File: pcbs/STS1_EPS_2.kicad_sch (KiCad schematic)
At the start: 1 part, among them J1 Inter-EPS

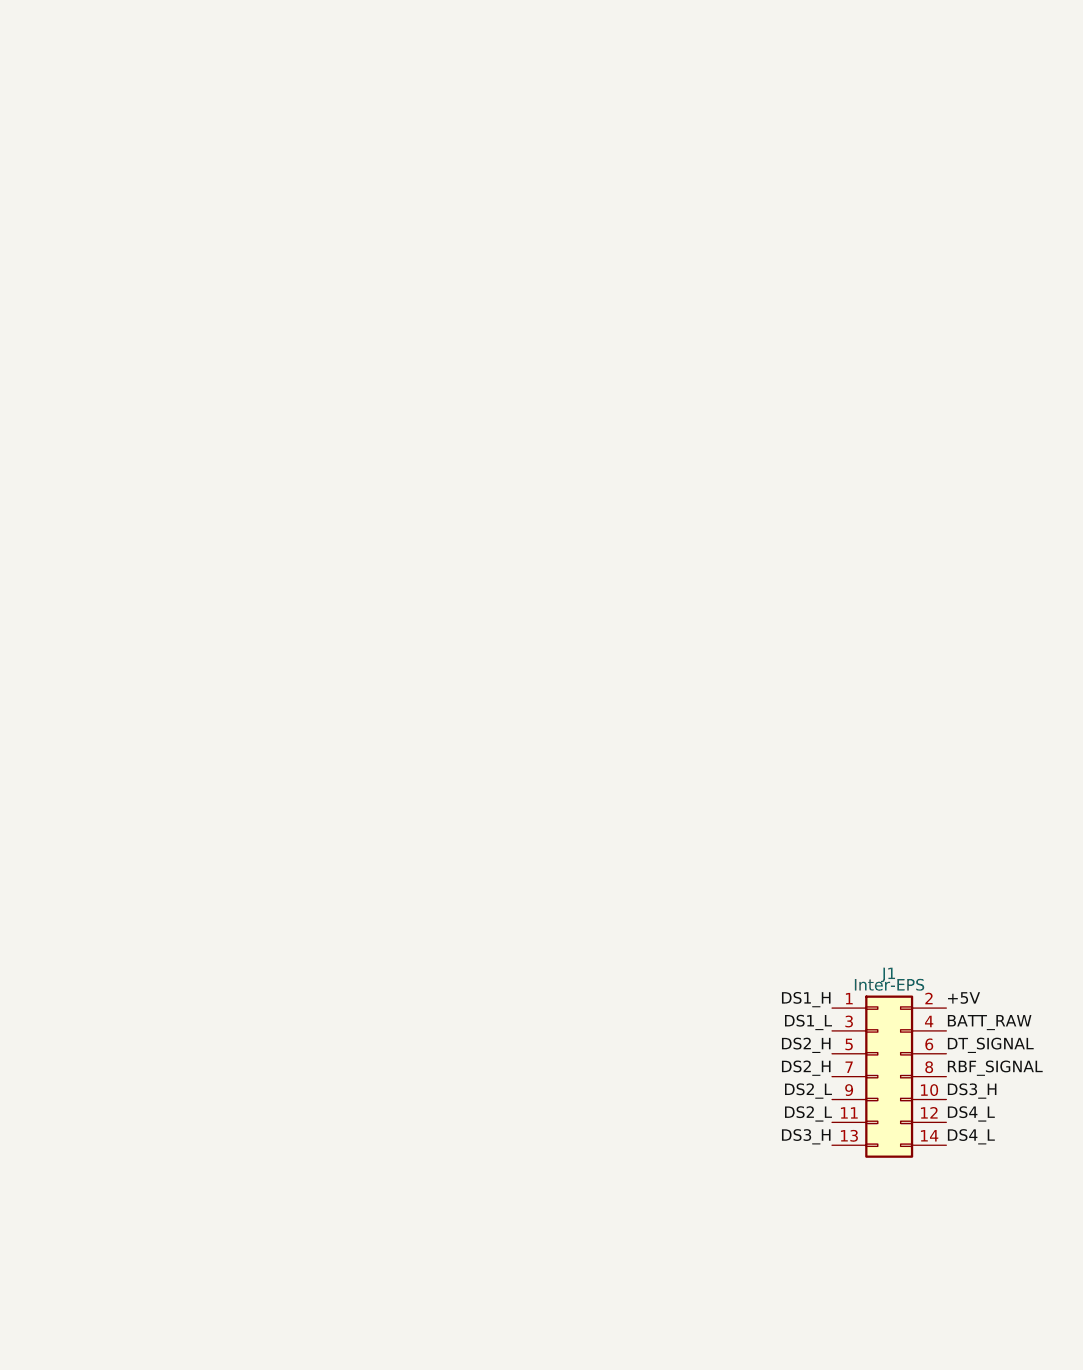
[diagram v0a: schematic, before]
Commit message: Worked on STS1_EPS_1 and began work on STS1_EPS_2.
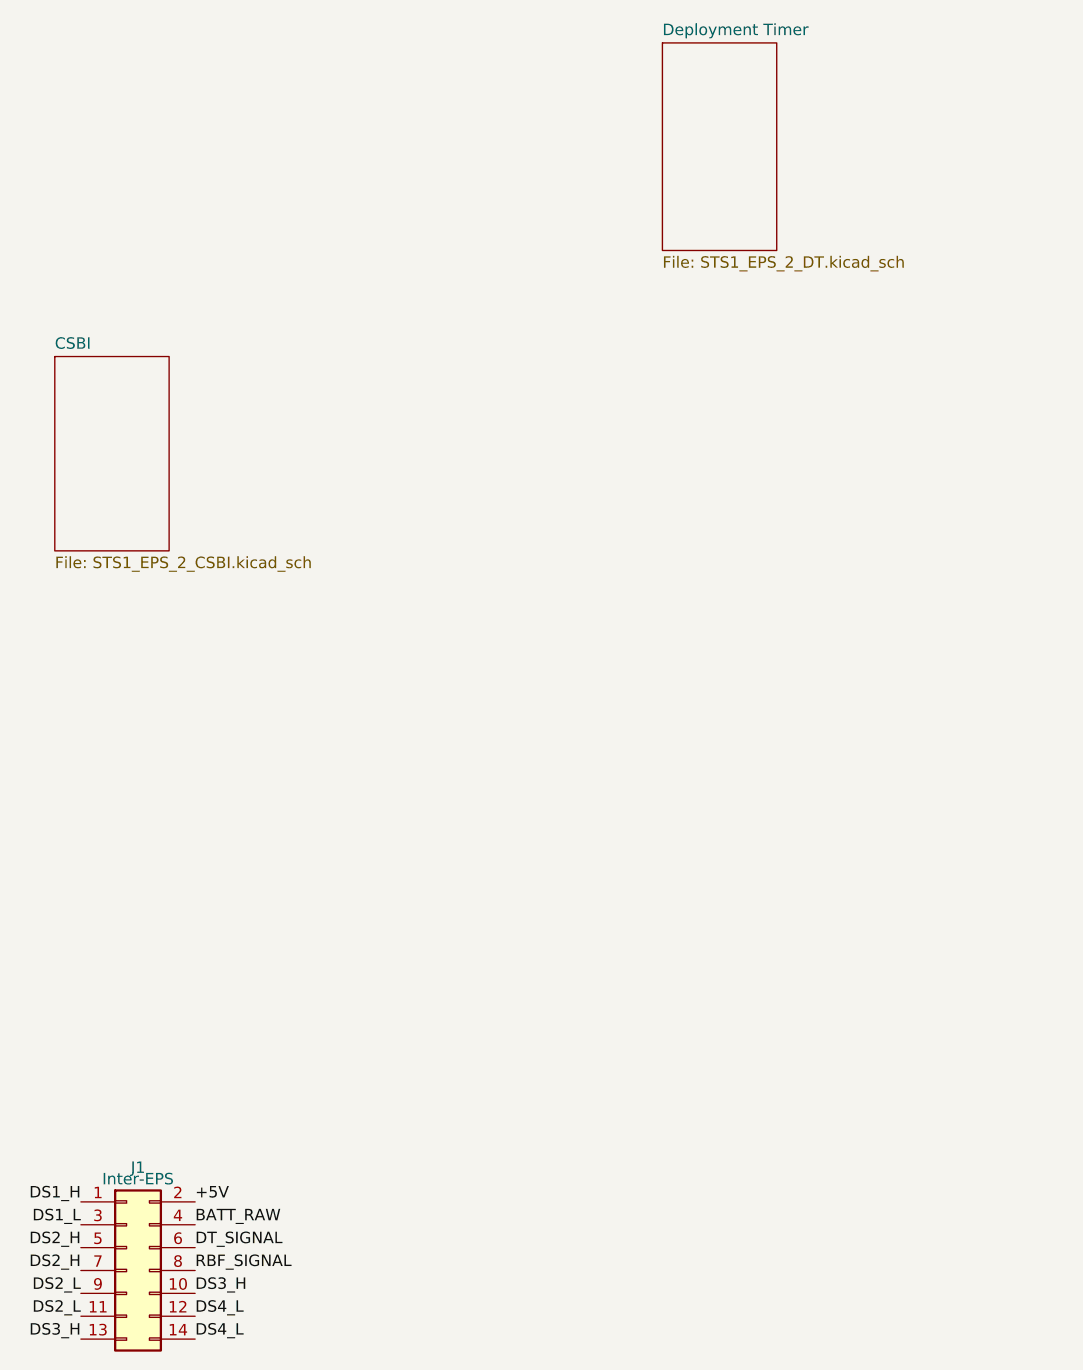
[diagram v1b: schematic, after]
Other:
- added sheet CSBI (STS1_EPS_2_CSBI.kicad_sch)
- added sheet Deployment Timer (STS1_EPS_2_DT.kicad_sch)
- moved on the sheet: J1
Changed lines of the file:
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@@
 (kicad_sch (version 20211123) (generator eeschema)
   (paper "A4")
-  (label "DS1_H" (at 120.65 149.86 180)
+  (label "DS1_H" (at 37.1856 171.3992 180)
     (effects (font (size 1.27 1.27)) (justify right bottom))
   )
-  (label "DS4_L" (at 133.35 162.56 0)
+  (label "DS4_L" (at 49.8856 184.0992 0)
     (effects (font (size 1.27 1.27)) (justify left bottom))
   )
-  (label "DT_SIGNAL" (at 133.35 154.94 0)
+  (label "DT_SIGNAL" (at 49.8856 176.4792 0)
     (effects (font (size 1.27 1.27)) (justify left bottom))
   )
-  (label "DS3_H" (at 120.65 165.1 180)
+  (label "DS3_H" (at 37.1856 186.6392 180)
     (effects (font (size 1.27 1.27)) (justify right bottom))
   )
-  (label "DS2_H" (at 120.65 157.48 180)
+  (label "DS2_H" (at 37.1856 179.0192 180)
     (effects (font (size 1.27 1.27)) (justify right bottom))
   )
-  (label "DS3_H" (at 133.35 160.02 0)
+  (label "DS3_H" (at 49.8856 181.5592 0)
     (effects (font (size 1.27 1.27)) (justify left bottom))
   )
-  (label "+5V" (at 133.35 149.86 0)
+  (label "+5V" (at 49.8856 171.3992 0)
     (effects (font (size 1.27 1.27)) (justify left bottom))
   )
-  (label "DS2_L" (at 120.65 160.02 180)
+  (label "DS2_L" (at 37.1856 181.5592 180)
     (effects (font (size 1.27 1.27)) (justify right bottom))
   )
-  (label "DS4_L" (at 133.35 165.1 0)
+  (label "DS4_L" (at 49.8856 186.6392 0)
     (effects (font (size 1.27 1.27)) (justify left bottom))
   )
-  (label "DS2_H" (at 120.65 154.94 180)
+  (label "DS2_H" (at 37.1856 176.4792 180)
     (effects (font (size 1.27 1.27)) (justify right bottom))
   )
-  (label "DS1_L" (at 120.65 152.4 180)
+  (label "DS1_L" (at 37.1856 173.9392 180)
     (effects (font (size 1.27 1.27)) (justify right bottom))
   )
-  (label "BATT_RAW" (at 133.35 152.4 0)
+  (label "BATT_RAW" (at 49.8856 173.9392 0)
     (effects (font (size 1.27 1.27)) (justify left bottom))
   )
-  (label "RBF_SIGNAL" (at 133.35 157.48 0)
+  (label "RBF_SIGNAL" (at 49.8856 179.0192 0)
     (effects (font (size 1.27 1.27)) (justify left bottom))
   )
-  (label "DS2_L" (at 120.65 162.56 180)
+  (label "DS2_L" (at 37.1856 184.0992 180)
     (effects (font (size 1.27 1.27)) (justify right bottom))
   )
-  (symbol (lib_id "Connector_Generic:Conn_02x07_Odd_Even") (at 125.73 157.48 0) (unit 1)
+  (symbol (lib_id "Connector_Generic:Conn_02x07_Odd_Even") (at 42.2656 179.0192 0) (unit 1)
     (in_bom yes) (on_board yes)
-    (property "Reference" "J1" (id 0) (at 127 146.05 0))
-    (property "Value" "Inter-EPS" (id 1) (at 127 147.32 0))
-    (property "Footprint" "Connector_PinHeader_2.00mm:PinHeader_2x07_P2.00mm_Vertical" (id 2) (at 125.73 157.48 0)
+    (property "Reference" "J1" (id 0) (at 43.5356 167.5892 0))
+    (property "Value" "Inter-EPS" (id 1) (at 43.5356 168.8592 0))
+    (property "Footprint" "Connector_PinHeader_2.00mm:PinHeader_2x07_P2.00mm_Vertical" (id 2) (at 42.2656 179.0192 0)
       (effects (font (size 1.27 1.27)) hide)
     )
-    (property "Datasheet" "~" (id 3) (at 125.73 157.48 0)
+    (property "Datasheet" "~" (id 3) (at 42.2656 179.0192 0)
       (effects (font (size 1.27 1.27)) hide)
     )
@@
     (pin "9")
   )
+  (sheet (at 34.29 77.47) (size 12.7 21.59) (fields_autoplaced)
+    (stroke (width 0.1524) (type solid) (color 0 0 0 0))
+    (fill (color 0 0 0 0.0000))
+    (property "Sheet name" "CSBI" (id 0) (at 34.29 76.7584 0)
+      (effects (font (size 1.27 1.27)) (justify left bottom))
+    )
+    (property "Sheet file" "STS1_EPS_2_CSBI.kicad_sch" (id 1) (at 34.29 99.6446 0)
+      (effects (font (size 1.27 1.27)) (justify left top))
+    )
+  )
+  (sheet (at 101.8032 42.6212) (size 12.7 23.0632) (fields_autoplaced)
+    (stroke (width 0.1524) (type solid) (color 0 0 0 0))
+    (fill (color 0 0 0 0.0000))
+    (property "Sheet name" "Deployment Timer" (id 0) (at 101.8032 41.9096 0)
+      (effects (font (size 1.27 1.27)) (justify left bottom))
+    )
+    (property "Sheet file" "STS1_EPS_2_DT.kicad_sch" (id 1) (at 101.8032 66.269 0)
+      (effects (font (size 1.27 1.27)) (justify left top))
+    )
+  )
   (sheet_instances
     (path "/" (page "1"))
+    (path "/565e35d1-cb7b-4a86-8e2f-32bed42f487e" (page "2"))
+    (path "/d08cc104-26df-403e-aeed-bb3c2e21e328" (page "3"))
   )
   (symbol_instances
+    (path "/565e35d1-cb7b-4a86-8e2f-32bed42f487e/00000000-0000-0000-0000-0000617ac8f5"
+      (reference "#PWR019") (unit 1) (value "~") (footprint "")
+    )
+    (path "/565e35d1-cb7b-4a86-8e2f-32bed42f487e/00000000-0000-0000-0000-0000617acff5"
+      (reference "#PWR020") (unit 1) (value "~") (footprint "")
+    )
+    (path "/565e35d1-cb7b-4a86-8e2f-32bed42f487e/00000000-0000-0000-0000-0000617ae72f"
+      (reference "#PWR021") (unit 1) (value "~") (footprint "")
+    )
+    (path "/565e35d1-cb7b-4a86-8e2f-32bed42f487e/00000000-0000-0000-0000-000062965f60"
+      (reference "#PWR022") (unit 1) (value "~") (footprint "")
+    )
+    (path "/565e35d1-cb7b-4a86-8e2f-32bed42f487e/00000000-0000-0000-0000-0000617b045a"
+      (reference "#PWR023") (unit 1) (value "~") (footprint "")
+    )
+    (path "/565e35d1-cb7b-4a86-8e2f-32bed42f487e/00000000-0000-0000-0000-00006298b185"
+      (reference "#PWR024") (unit 1) (value "~") (footprint "")
+    )
+    (path "/565e35d1-cb7b-4a86-8e2f-32bed42f487e/00000000-0000-0000-0000-0000617b9d0c"
+      (reference "#PWR025") (unit 1) (value "~") (footprint "")
+    )
+    (path "/565e35d1-cb7b-4a86-8e2f-32bed42f487e/00000000-0000-0000-0000-0000617ba312"
+      (reference "#PWR026") (unit 1) (value "~") (footprint "")
+    )
+    (path "/565e35d1-cb7b-4a86-8e2f-32bed42f487e/00000000-0000-0000-0000-0000617c375f"
+      (reference "#PWR027") (unit 1) (value "~") (footprint "")
+    )
+    (path "/565e35d1-cb7b-4a86-8e2f-32bed42f487e/00000000-0000-0000-0000-0000617c40ab"
+      (reference "#PWR028") (unit 1) (value "~") (footprint "")
+    )
+    (path "/565e35d1-cb7b-4a86-8e2f-32bed42f487e/00000000-0000-0000-0000-000062992e45"
+      (reference "#PWR029") (unit 1) (value "~") (footprint "")
+    )
+    (path "/565e35d1-cb7b-4a86-8e2f-32bed42f487e/00000000-0000-0000-0000-0000617de51f"
+      (reference "#PWR030") (unit 1) (value "~") (footprint "")
+    )
+    (path "/565e35d1-cb7b-4a86-8e2f-32bed42f487e/00000000-0000-0000-0000-0000617db593"
+      (reference "#PWR031") (unit 1) (value "~") (footprint "")
+    )
+    (path "/565e35d1-cb7b-4a86-8e2f-32bed42f487e/00000000-0000-0000-0000-00006180bd18"
+      (reference "#PWR032") (unit 1) (value "~") (footprint "")
+    )
+    (path "/565e35d1-cb7b-4a86-8e2f-32bed42f487e/00000000-0000-0000-0000-0000617c4e49"
+      (reference "#PWR033") (unit 1) (value "~") (footprint "")
+    )
+    (path "/565e35d1-cb7b-4a86-8e2f-32bed42f487e/00000000-0000-0000-0000-0000617c4645"
+      (reference "#PWR034") (unit 1) (value "~") (footprint "")
+    )
+    (path "/565e35d1-cb7b-4a86-8e2f-32bed42f487e/00000000-0000-0000-0000-00006179b797"
+      (reference "CSBI_1") (unit 1) (value "~") (footprint "Connector_PinHeader_2.00mm:PinHeader_2x25_P2.00mm_Vertical")
+    )
+    (path "/565e35d1-cb7b-4a86-8e2f-32bed42f487e/00000000-0000-0000-0000-0000617ab6cd"
+      (reference "CSBI_2") (unit 1) (value "~") (footprint "Connector_PinHeader_2.00mm:PinHeader_2x25_P2.00mm_Vertical")
+    )
     (path "/3cc4c0a7-4616-4293-936d-f8a3bdd480dc"
       (reference "J1") (unit 1) (value "Inter-EPS") (footprint "Connector_PinHeader_2.00mm:PinHeader_2x07_P2.00mm_Vertical")
     )
+    (path "/d08cc104-26df-403e-aeed-bb3c2e21e328/2680cefe-13e2-4d80-ac91-b159847b7c22"
+      (reference "U?") (unit 1) (value "LTC6995HS6-1#TRMPBF") (footprint "SOT95P280X100-6N")
+    )
   )

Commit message: Finished first revision of schematic.
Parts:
- added J2: DS1, STS_Connector:M808420245, symbol Connector_Generic:Conn_01x02
- added J3: DS2, STS_Connector:M808420245, symbol Connector_Generic:Conn_01x02
- added J4: DS3, STS_Connector:M808420245, symbol Connector_Generic:Conn_01x02
- added J5: DS4, STS_Connector:M808420245, symbol Connector_Generic:Conn_01x02
- added J6: RBF, STS_Connector:M808420245, symbol Connector_Generic:Conn_01x02
- added J7: Antenna Deployment, STS_Connector:M80-85104YY, symbol Connector_Generic:Conn_02x02_Odd_Even
- added J8: UCI, STS_Connector:M80-85110YY, symbol Connector_Generic:Conn_02x05_Odd_Even
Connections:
- net DS1_L is gone; now on net INTERNAL_V: J1.3 (Pin_3)
- net DS2_H is gone; now on net INTERNAL_V: J1.5 (Pin_5), J1.7 (Pin_7)
- net DT_SIGNAL is gone; now on net BATT_RAW: J1.6 (Pin_6)
- net BATT_RAW: now also J8.1 (Pin_1), J8.2 (Pin_2), J8.3 (Pin_3), J8.4 (Pin_4)
- net DS1_H renamed INTERNAL_V
- net DS2_L renamed DS1_SIGNAL_1
- net DS1_SIGNAL_1: no longer J1.11 (Pin_11)
- net DS3_H renamed DS2_SIGNAL_1
- net DS2_SIGNAL_1: no longer J1.13 (Pin_13)
- net DS4_L renamed GND
- net GND: now also J1.11 (Pin_11), J1.13 (Pin_13), J8.5 (Pin_5), J8.6 (Pin_6), J8.9 (Pin_9)
- net RBF_SIGNAL renamed VOUT_I
- new net Antenna Deployment/ANT_DEPLOY+: J7.1 (Pin_1), J7.2 (Pin_2)
- new net Antenna Deployment/ANT_DEPLOY-: J7.3 (Pin_3), J7.4 (Pin_4)
- new net Deployment Switches + RBF/DS1+: J2.1 (Pin_1)
- new net Deployment Switches + RBF/DS1-: J2.2 (Pin_2)
- new net Deployment Switches + RBF/DS2+: J3.1 (Pin_1)
- new net Deployment Switches + RBF/DS2-: J3.2 (Pin_2)
- new net Deployment Switches + RBF/DS3+: J4.1 (Pin_1)
- new net Deployment Switches + RBF/DS3-: J4.2 (Pin_2)
- new net Deployment Switches + RBF/DS4+: J5.1 (Pin_1)
- new net Deployment Switches + RBF/DS4-: J5.2 (Pin_2)
- new net Deployment Switches + RBF/RBF+: J6.1 (Pin_1)
- new net Deployment Switches + RBF/RBF-: J6.2 (Pin_2)
- new net UCI_COBC_UART_1: J8.7 (Pin_7)
- new net UCI_COBC_UART_2: J8.8 (Pin_8)
- no-connect marks 0 -> 1
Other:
- added sheet Antenna Deployment (STS1_EPS_ANT_DEPLOY.kicad_sch)
- added sheet Battery State Detection (STS1_EPS_2_BAT_STATE.kicad_sch)
- added sheet Bus Gate (STS1_EPS_2_BUS_GATE.kicad_sch)
- added sheet Deployment Switches + RBF (STS1_EPS_2_DS_RBF.kicad_sch)
- sheet CSBI ports: added EPS_ANT_DEPLOY, EPS_BAT_FAULT, EPS_BAT_GOOD, UCI_COBC_UART[1..2], VOUT; removed none
- sheet Deployment Timer ports: added +5V, DS1_SIGNAL, DS2_SIGNAL, DS3_SIGNAL, DS4_SIGNAL, DT_SIGNAL, RBF_SIGNAL; removed none

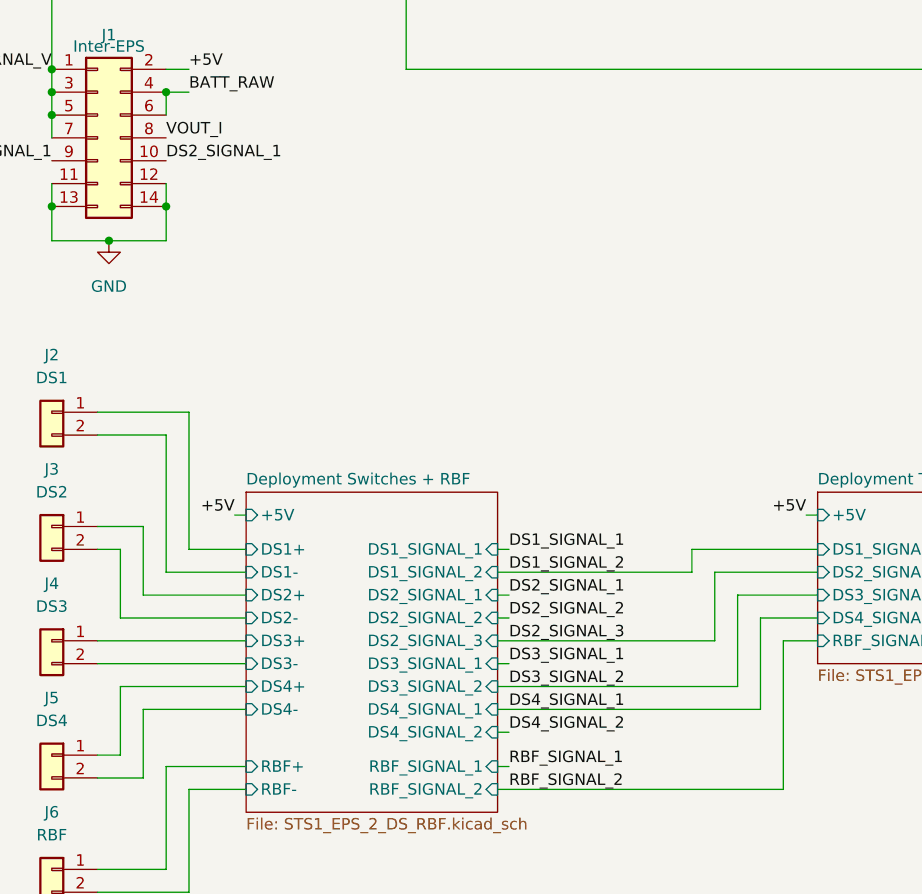
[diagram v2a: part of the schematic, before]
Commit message: Worked on STS1_EPS_2 layout.
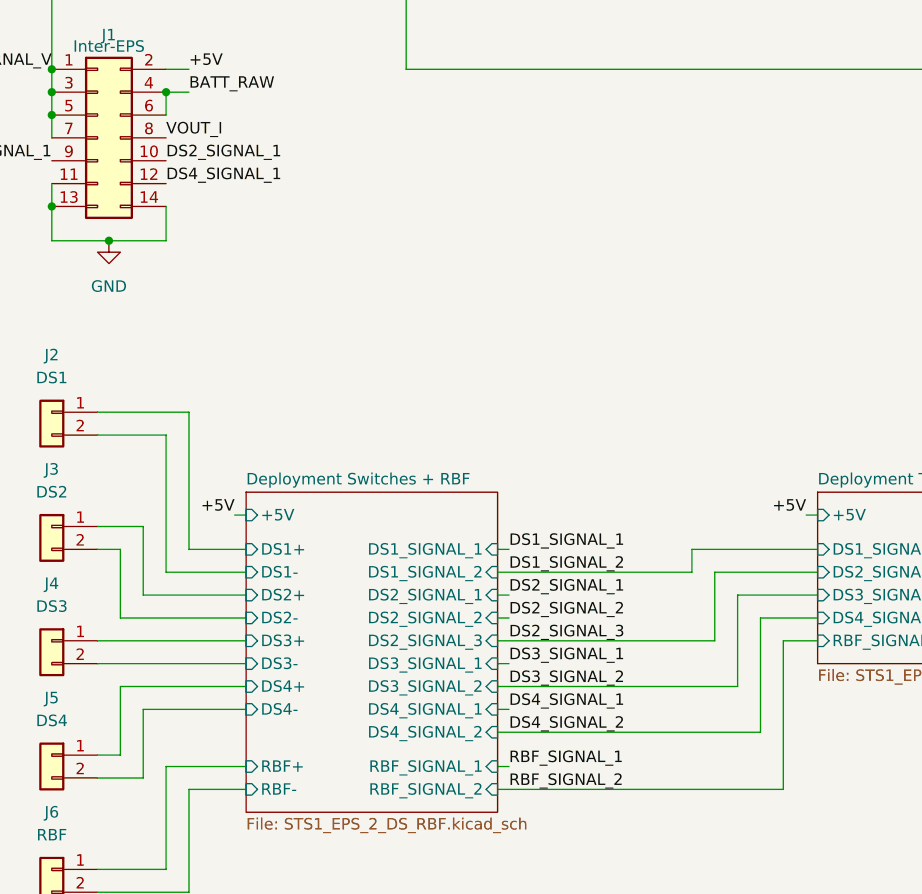
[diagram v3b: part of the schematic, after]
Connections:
- net DS4_SIGNAL_1: now also J1.12 (Pin_12)
- net GND: no longer J1.12 (Pin_12)
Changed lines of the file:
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@@
   (junction (at 35.56 147.32) (diameter 0) (color 0 0 0 0)
-  )
-  (junction (at 40.64 58.42) (diameter 0) (color 0 0 0 0)
   )
   (junction (at 35.56 149.86) (diameter 0) (color 0 0 0 0)
@@
     (stroke (width 0) (type default) (color 0 0 0 0))
   )
-  (wire (pts (xy 77.47 114.3) (xy 106.68 114.3))
+  (wire (pts (xy 77.47 114.3) (xy 78.74 114.3))
     (stroke (width 0) (type default) (color 0 0 0 0))
   )
@@
     (stroke (width 0) (type default) (color 0 0 0 0))
   )
-  (wire (pts (xy 77.47 116.84) (xy 78.74 116.84))
+  (wire (pts (xy 77.47 116.84) (xy 106.68 116.84))
     (stroke (width 0) (type default) (color 0 0 0 0))
   )
@@
     (stroke (width 0) (type default) (color 0 0 0 0))
   )
-  (wire (pts (xy 40.64 55.88) (xy 40.64 58.42))
-    (stroke (width 0) (type default) (color 0 0 0 0))
-  )
   (wire (pts (xy 38.1 93.98) (xy 38.1 101.6))
     (stroke (width 0) (type default) (color 0 0 0 0))
@@
     (stroke (width 0) (type default) (color 0 0 0 0))
   )
-  (wire (pts (xy 106.68 114.3) (xy 106.68 104.14))
+  (wire (pts (xy 106.68 104.14) (xy 106.68 116.84))
     (stroke (width 0) (type default) (color 0 0 0 0))
   )
@@
     (effects (font (size 1.27 1.27)) (justify right bottom))
   )
+  (label "DS4_SIGNAL_1" (at 40.64 55.88 0)
+    (effects (font (size 1.27 1.27)) (justify left bottom))
+  )
   (label "DS2_SIGNAL_3" (at 78.74 106.68 0)
